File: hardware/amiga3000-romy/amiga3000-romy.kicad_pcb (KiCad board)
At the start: 2 copper layers, 40.1 x 55.5 mm, 5 parts

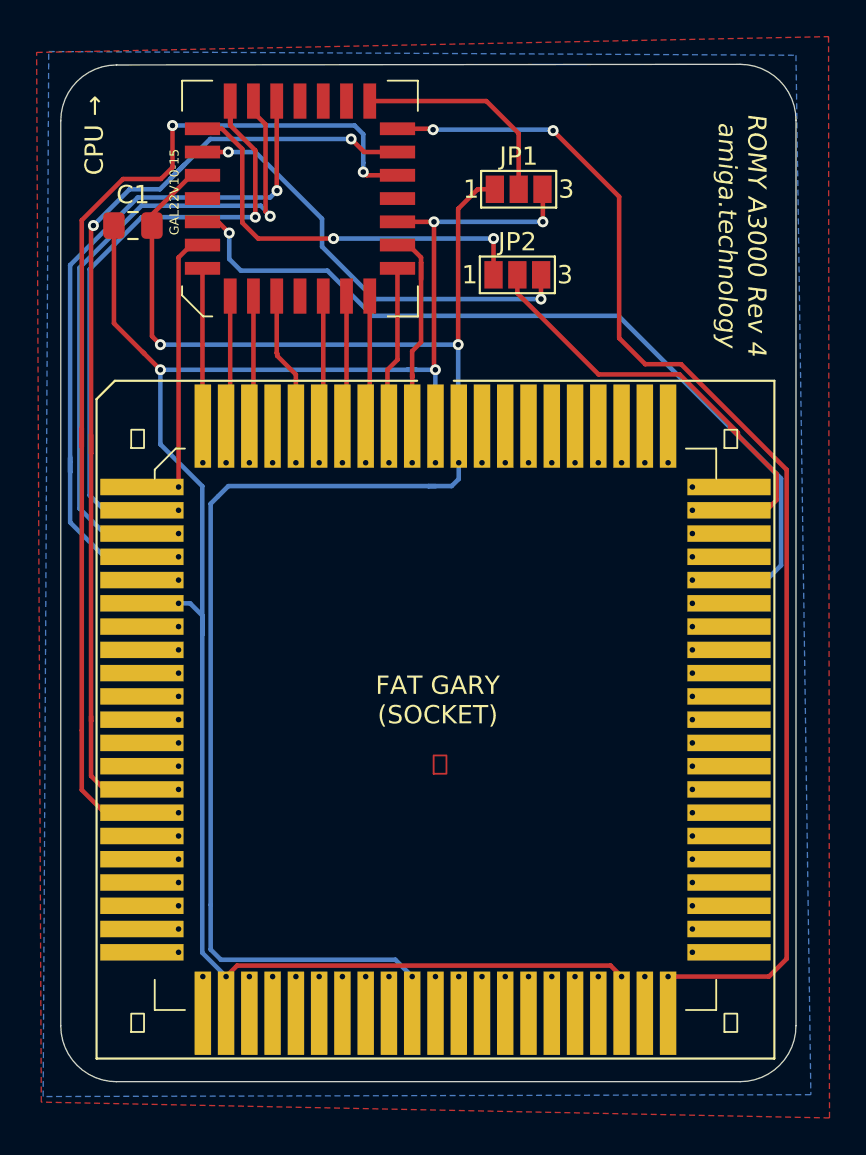
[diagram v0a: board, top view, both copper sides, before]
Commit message: Update Amiga3000 ROMY to Rev4a
major difference is the address header to support 4MB ROMs
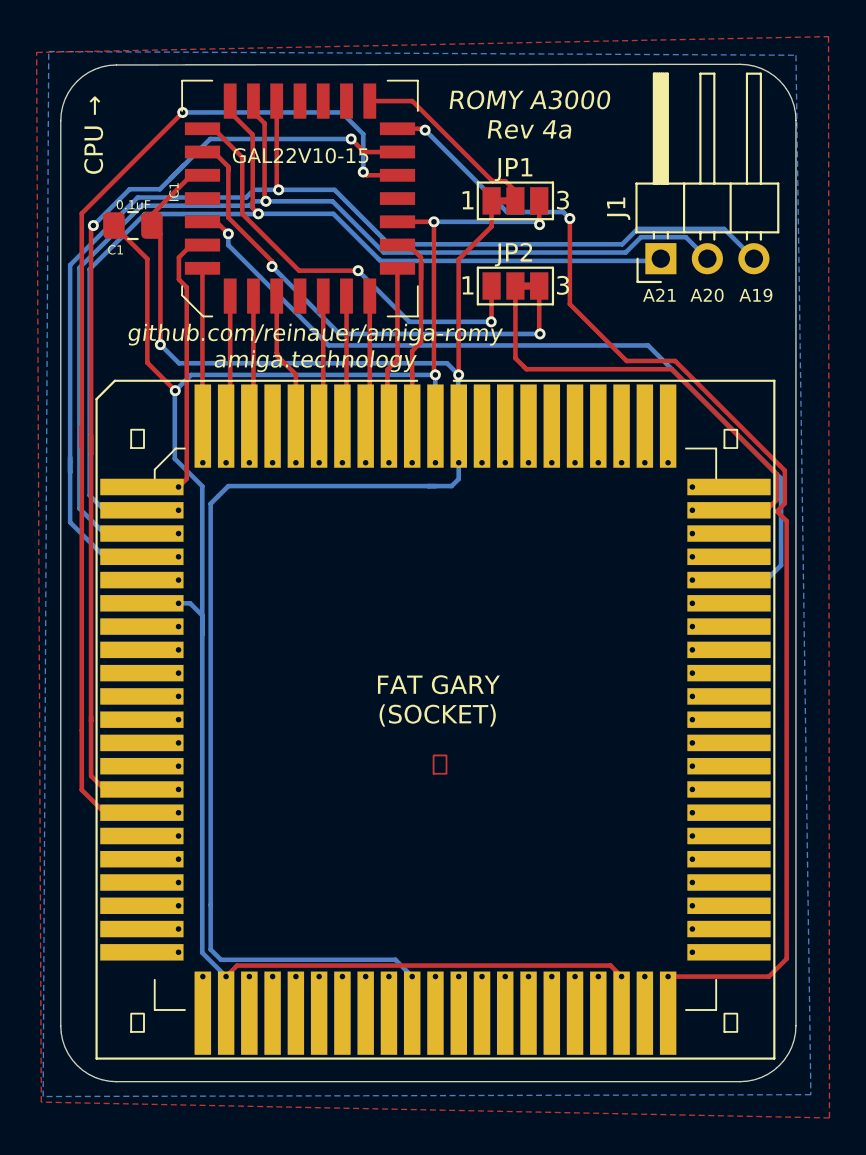
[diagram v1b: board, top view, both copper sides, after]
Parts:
- added J1: Conn_01x03_Male, Connector_PinHeader_2.54mm:PinHeader_1x03_P2.54mm_Horizontal, F.Cu at (117.8, 41.4)
- IC2: renamed from  
- JP1: footprint Jumper:SolderJumper-3_P1.3mm_Open_Pad1.0x1.5mm_NumberLabels -> amiga-romy:SolderJumper-3_P1.3mm_Closed_12_Pad1.0x1.5mm_NumberLabels
- JP2: footprint Jumper:SolderJumper-3_P1.3mm_Open_Pad1.0x1.5mm_NumberLabels -> amiga-romy:SolderJumper-3_P1.3mm_Closed_23_Pad1.0x1.5mm_NumberLabels
- moved JP1 0.66 mm to (109.9, 38.3)
- moved JP2 0.62 mm to (109.9, 42.9)
- renumbered GAL22V10-15 to IC1
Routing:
- net Net-(IC1-Pad23): track 39.4 -> 67.7 mm
- net Net-(IC1-Pad24): track 38.5 -> 63.3 mm
- net Net-(IC1-Pad25): track 36.0 -> 57.9 mm
- net Net-(IC1-Pad27): track 24.1 -> 27.8 mm
- net Net-(C1-Pad1): track 111.6 -> 109.9 mm
- net Net-(IC1-Pad26): track 24.0 -> 25.5 mm
- net Net-(IC1-Pad18): track 67.1 -> 65.5 mm
- net Net-(IC2-Pad73): track 26.2 -> 27.7 mm
- net Net-(IC1-Pad19): track 11.9 -> 10.5 mm
- net Net-(C1-Pad2): track 99.0 -> 98.4 mm
- net Net-(IC1-Pad16): track 61.0 -> 60.4 mm
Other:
- board text added: "A19"
- board text added: "A20"
- board text added: "A21"
- board text added: "CREDITS GO TO SPEEDGEEK, COSMOS, ACILL, FLOREN, CDH"
- board text added: "ROMY A3000 Rev 4a"
- board text added: "github.com/reinauer/amiga-romy amiga.technology"
- board text removed: "GREETINGS TO SPEEDGEEK, COSMOS, ACILL, FLOREN"
- board text removed: "ROMY A3000 Rev 4 amiga.technology"
- board text removed: "https://github.com/reinauer/amiga-romy/"
